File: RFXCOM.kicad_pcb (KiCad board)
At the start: 2 copper layers, 101 x 77 mm, 33 parts, among them J1 TX Antenna, J2 RX Antenna, J3 SWD_Connector, J4 Rx, J5 Tx, J6 USB_C_Receptacle_USB2.0, J7 SWD, U1 STM32L412KBTx, U2 USBLC6-2SC6, U3 LD2981ABU33TR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

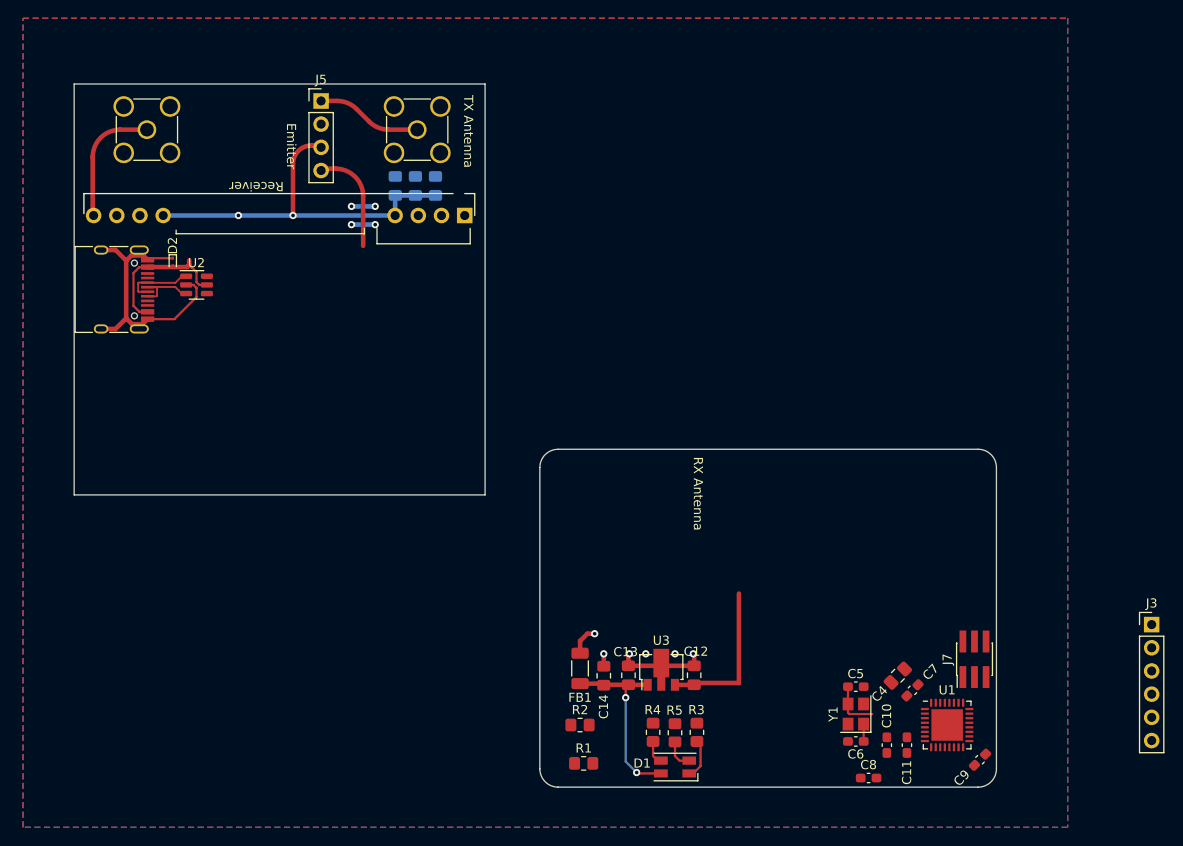
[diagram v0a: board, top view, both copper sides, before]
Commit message: add cc110L
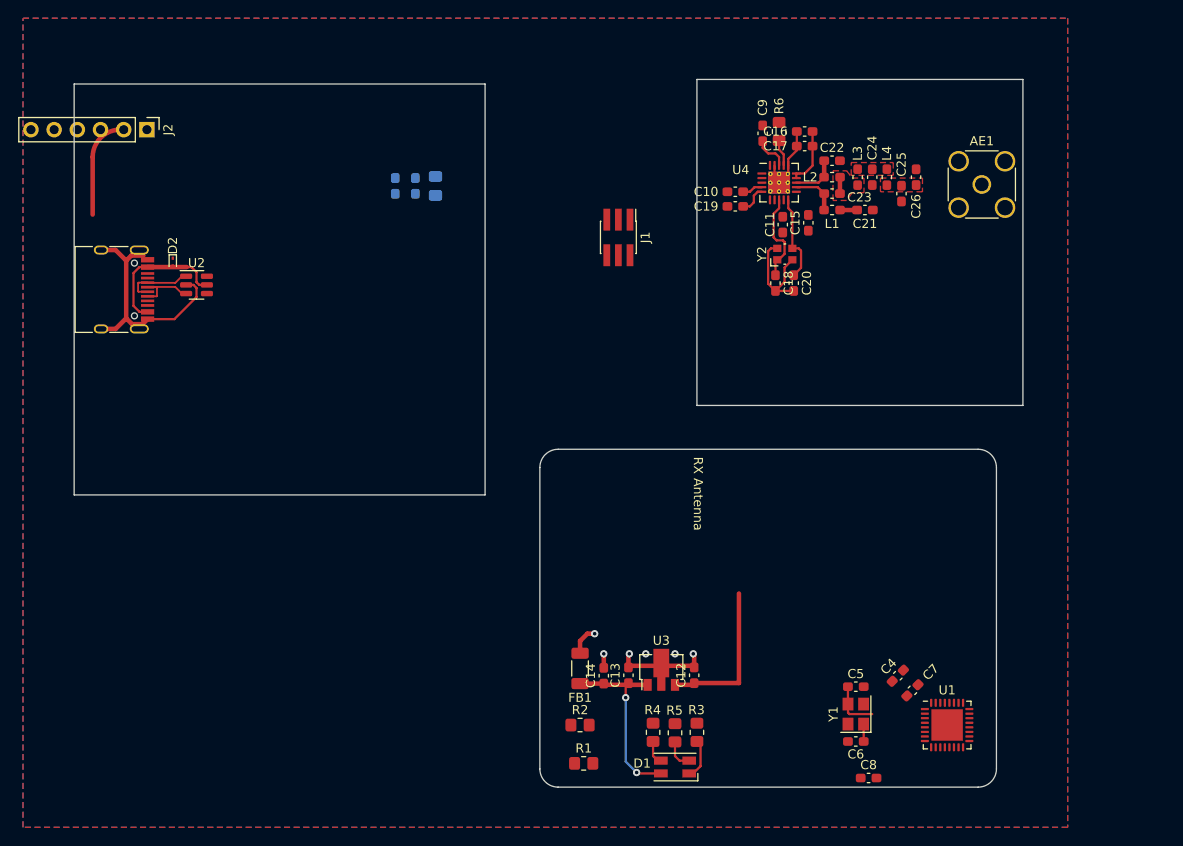
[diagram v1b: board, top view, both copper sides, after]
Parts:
- removed J3: SWD_Connector, Connector_PinHeader_2.54mm:PinHeader_1x06_P2.54mm_Vertical
- removed J4: Rx, rf_components:RXB6
- removed J5: Tx, Connector_PinHeader_2.54mm:PinHeader_1x04_P2.54mm_Vertical
- removed J7: SWD, Connector_PinHeader_1.27mm:PinHeader_2x03_P1.27mm_Vertical_SMD
- added AE1: Antenna_Shield, Connector_Coaxial:SMA_Amphenol_132134_Vertical, F.Cu at (144.4, 36.0)
- added C15: 100n, Capacitor_SMD:C_0603_1608Metric_Pad1.08x0.95mm_HandSolder, F.Cu at (125.4, 40.2)
- added C16: 100n, Capacitor_SMD:C_0603_1608Metric_Pad1.08x0.95mm_HandSolder, F.Cu at (125.0, 30.2)
- added C17: 100n, Capacitor_SMD:C_0603_1608Metric_Pad1.08x0.95mm_HandSolder, F.Cu at (125.0, 31.8)
- added C18: 22pF, Capacitor_SMD:C_0603_1608Metric_Pad1.08x0.95mm_HandSolder, F.Cu at (121.8, 46.8)
- added C19: 100n, Capacitor_SMD:C_0603_1608Metric_Pad1.08x0.95mm_HandSolder, F.Cu at (117.4, 38.4)
- added C20: 22pF, Capacitor_SMD:C_0603_1608Metric_Pad1.08x0.95mm_HandSolder, F.Cu at (123.8, 46.8)
- added C21: 220pF, Capacitor_SMD:C_0603_1608Metric_Pad1.08x0.95mm_HandSolder, F.Cu at (131.6, 38.8)
- added C22: 3.9pF, Capacitor_SMD:C_0603_1608Metric_Pad1.08x0.95mm_HandSolder, F.Cu at (128.0, 33.4)
- added C23: 3.9pF, Capacitor_SMD:C_0603_1608Metric_Pad1.08x0.95mm_HandSolder, F.Cu at (128.0, 37.0)
- added C24: 8.2pF, Capacitor_SMD:C_0603_1608Metric_Pad1.08x0.95mm_HandSolder, F.Cu at (132.4, 35.2)
- added C25: 5.6pf, Capacitor_SMD:C_0603_1608Metric_Pad1.08x0.95mm_HandSolder, F.Cu at (135.6, 37.0)
- added C26: 0.9pF, Capacitor_SMD:C_0603_1608Metric_Pad1.08x0.95mm_HandSolder, F.Cu at (137.2, 35.2)
- added L1: 27nH, Inductor_SMD:L_0603_1608Metric_Pad1.05x0.95mm_HandSolder, F.Cu at (128.0, 38.8)
- added L2: 27nH, Inductor_SMD:L_0603_1608Metric_Pad1.05x0.95mm_HandSolder, F.Cu at (128.0, 35.2)
- added L3: 22nH, Inductor_SMD:L_0603_1608Metric_Pad1.05x0.95mm_HandSolder, F.Cu at (130.8, 35.2)
- added L4: 27nH, Inductor_SMD:L_0603_1608Metric_Pad1.05x0.95mm_HandSolder, F.Cu at (134.0, 35.2)
- added R6: 56k, Resistor_SMD:R_0805_2012Metric_Pad1.20x1.40mm_HandSolder, F.Cu at (122.2, 30.2)
- added U4: CC110L, Package_DFN_QFN:Texas_S-PVQFN-N20_EP2.4x2.4mm_ThermalVias, F.Cu at (122.2, 35.8)
- added Y2: 26M, Crystal:Crystal_SMD_Abracon_ABM10-4Pin_2.5x2.0mm, F.Cu at (122.8, 43.6)
- C1: value 100n -> 4u7
- C10: value 1u -> 100n
- C11: value 10n -> 100n
- C12, C13, C14: footprint Capacitor_SMD:C_0805_2012Metric_Pad1.18x1.45mm_HandSolder -> Capacitor_SMD:C_0603_1608Metric_Pad1.08x0.95mm_HandSolder
- C2: value 470n -> 100n; footprint Capacitor_SMD:C_0805_2012Metric_Pad1.18x1.45mm_HandSolder -> Capacitor_SMD:C_0603_1608Metric_Pad1.08x0.95mm_HandSolder
- C3: value 10u -> 100n; footprint Capacitor_SMD:C_0805_2012Metric_Pad1.18x1.45mm_HandSolder -> Capacitor_SMD:C_0603_1608Metric_Pad1.08x0.95mm_HandSolder
- C4: value 4u7 -> 10p; footprint Capacitor_SMD:C_0805_2012Metric_Pad1.18x1.45mm_HandSolder -> Capacitor_SMD:C_0603_1608Metric_Pad1.08x0.95mm_HandSolder
- C6: value 10p -> 1u
- C8: value 100n -> 10n
- J1: value TX Antenna -> SWD; footprint Connector_Coaxial:SMA_Amphenol_901-144_Vertical -> Connector_PinHeader_1.27mm:PinHeader_2x03_P1.27mm_Vertical_SMD
- J2: value RX Antenna -> SWD_Connector; footprint Connector_Coaxial:SMA_Amphenol_901-144_Vertical -> Connector_PinHeader_2.54mm:PinHeader_1x06_P2.54mm_Vertical
- moved C9 72.6 mm to (120.4, 30.4), turned to -90 degrees
- moved C10 62.8 mm to (117.4, 36.8), turned to 0 degrees
- moved C11 58.6 mm to (122.6, 40.4), turned to 90 degrees
- moved J1 25.0 mm to (104.6, 41.8)
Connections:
- net /BOOT0 renamed /MCU/BOOT0
- net /USB_D+ renamed /MCU/USB_D+
- net /USB_D- renamed /MCU/USB_D-
- C1 pad 1: +5V -> +3.3V
- C10 pad 1: +3.3VA -> GND
- C10 pad 2: GND -> +3.3V
- C11 pad 1: +3.3VA -> GND
- C11 pad 2: GND -> +3.3V
- C2 pad 1: +5V -> +3.3V
- C3 pad 1: +5V -> +3.3V
- C4 pad 1: +3.3V -> GND
- C4 pad 2: GND -> Net-(C4-Pad2)
- C6 pad 1: GND -> +3.3VA
- C6 pad 2: Net-(C6-Pad2) -> GND
- C7 pad 1: +3.3V -> GND
- C7 pad 2: GND -> /MCU/~{RST}
- C8 pad 1: GND -> +3.3VA
- C8 pad 2: /~{RST} -> GND
- C9 pad 1: +3.3V -> GND
- C9 pad 2: GND -> +3.3V
- J1 pad 1: Net-(J1-Pad1) -> +3.3V
- J1 pad 2: GND -> /MCU/SWDIO
- J2 pad 1: /antenne -> unconnected-(J2-Pad1)
- J2 pad 2: GND -> /MCU/SWCLK
- U1 pad 10: /Rx_DER -> /MCU/Rx_DER
- U1 pad 2: Net-(C5-Pad2) -> Net-(C4-Pad2)
- U1 pad 23: /SWDIO -> /MCU/SWDIO
- U1 pad 24: /SWCLK -> /MCU/SWCLK
- U1 pad 26: /SWO -> /MCU/SWO
- U1 pad 3: Net-(C6-Pad2) -> Net-(C5-Pad2)
- U1 pad 4: /~{RST} -> /MCU/~{RST}
- U1 pad 8: /Tx_DATA -> /MCU/Tx_DATA
- U1 pad 9: /Rx_DATA -> /MCU/Rx_DATA
- Y1 pad 1: Net-(C6-Pad2) -> Net-(C5-Pad2)
- Y1 pad 3: Net-(C5-Pad2) -> Net-(C4-Pad2)
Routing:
- net +5V: track 77.5 -> 34.5 mm, vias 2 -> 0
- net GND: track 46.1 -> 60.0 mm, vias 9 -> 5
- net /antenne: track 13.8 -> 0.00 mm
- net +3.3V: track 19.7 -> 32.2 mm
- net /Tx_DATA: track 11.7 -> 0.00 mm
- net Net-(J1-Pad1): track 11.5 -> 0.00 mm
- net /MCU/SWCLK: track 0.00 -> 10.9 mm
- net Net-(U4-Pad8): track 0.00 -> 9.91 mm
- net Net-(U4-Pad10): track 0.00 -> 9.57 mm
- net Net-(C5-Pad2): track 5.55 -> 0.00 mm
- net Net-(C4-Pad2): track 0.00 -> 5.55 mm
- net Net-(C23-Pad1): track 0.00 -> 5.15 mm
- net Net-(C22-Pad1): track 0.00 -> 5.09 mm
- net Net-(C19-Pad2): track 0.00 -> 3.14 mm
- net Net-(R6-Pad1): track 0.00 -> 2.92 mm
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- added copper zone on F.Cu, net Net-(C23-Pad2)
- added copper zone on F.Cu, net Net-(C26-Pad1)
- added copper zone on F.Cu, net Net-(L3-Pad1)
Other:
- board size 101 x 77 mm -> 103.9 x 77.5 mm
- board text removed: "100n 470n 10µ"
- board text removed: "Emitter"
- board text removed: "Receiver"
- board text removed: "TX Antenna"
